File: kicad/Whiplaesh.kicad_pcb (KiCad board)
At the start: 2 copper layers, 257.1 x 106.2 mm, 88 parts, among them SW1 SW_PUSH, SW10 SW_PUSH, SW11 SW_PUSH, SW12 SW_PUSH, SW13 SW_PUSH, SW14 SW_PUSH, SW15 SW_PUSH, SW16 SW_PUSH, SW17 SW_PUSH, SW18 SW_PUSH, SW19 SW_PUSH, SW2 SW_PUSH, SW20 SW_PUSH, SW21 SW_PUSH, SW22 SW_PUSH, SW23 SW_PUSH, SW24 SW_PUSH, SW25 SW_PUSH, SW26 SW_PUSH, SW27 SW_PUSH, SW28 SW_PUSH, SW29 SW_PUSH, SW3 SW_PUSH, SW30 SW_PUSH, SW31 SW_PUSH, SW32 SW_PUSH, SW4 SW_PUSH, SW5 SW_PUSH, SW6 SW_PUSH, SW7 SW_PUSH, SW8 SW_PUSH, SW9 SW_PUSH

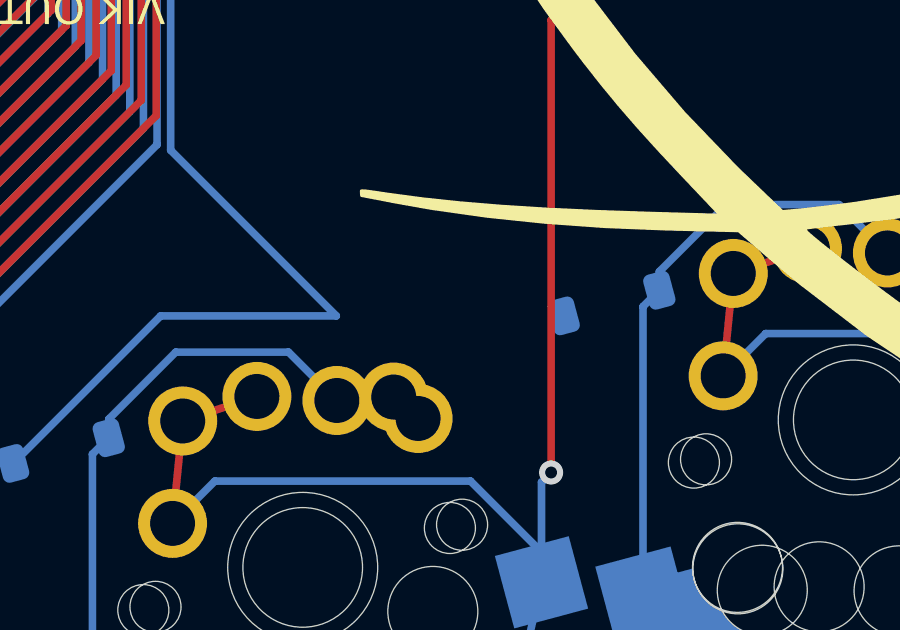
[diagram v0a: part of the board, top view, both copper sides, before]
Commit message: Add missing trace
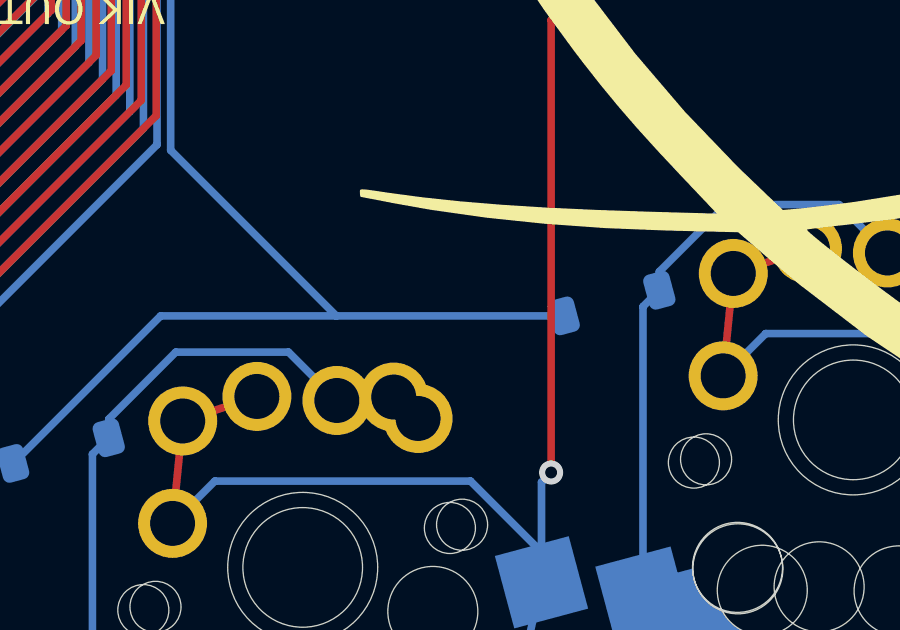
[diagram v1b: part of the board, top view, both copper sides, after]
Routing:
- net ROW3_r: track 72.7 -> 80.4 mm
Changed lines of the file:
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@@
+	)
+	(segment
+		(start 181.39 116.25)
+		(end 181.330511 116.309489)
+		(width 0.254)
+		(layer "B.Cu")
+		(net 49)
+	)
+	(segment
+		(start 181.398813 116.258813)
+		(end 181.39 116.25)
+		(width 0.254)
+		(layer "B.Cu")
+		(net 49)
+	)
+	(segment
+		(start 181.398813 116.309488)
+		(end 181.398813 116.258813)
+		(width 0.254)
+		(layer "B.Cu")
+		(net 49)
+	)
+	(segment
+		(start 181.330511 116.309489)
+		(end 173.819489 116.309489)
+		(width 0.254)
+		(layer "B.Cu")
+		(net 49)
 	)
 	(segment
